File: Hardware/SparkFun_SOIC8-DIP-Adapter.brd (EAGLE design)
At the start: 20.8 x 20.8 mm, 17 parts, among them U1 GENERIC-SOIC8, U2 GENERIC-SOIC8, U3 GENERIC-SOIC8, U4 GENERIC-SOIC8

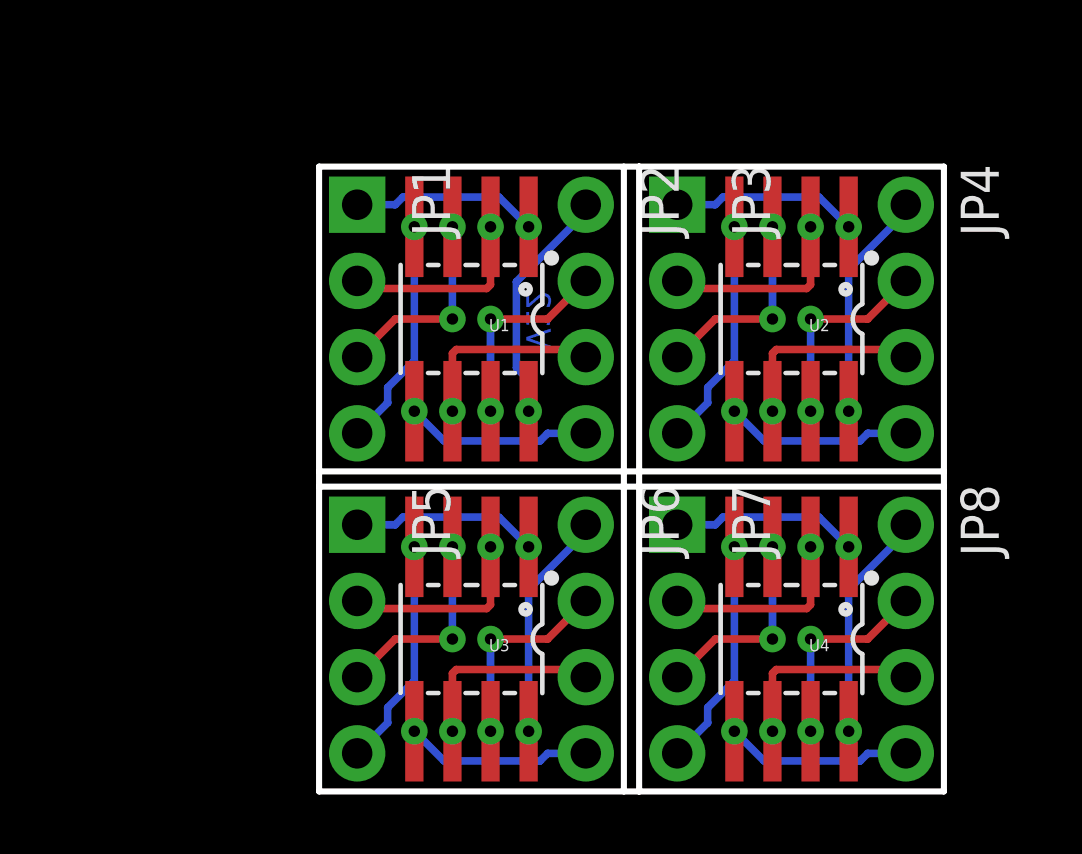
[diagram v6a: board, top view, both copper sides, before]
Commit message: added simple text to dimension layer noting v-scores
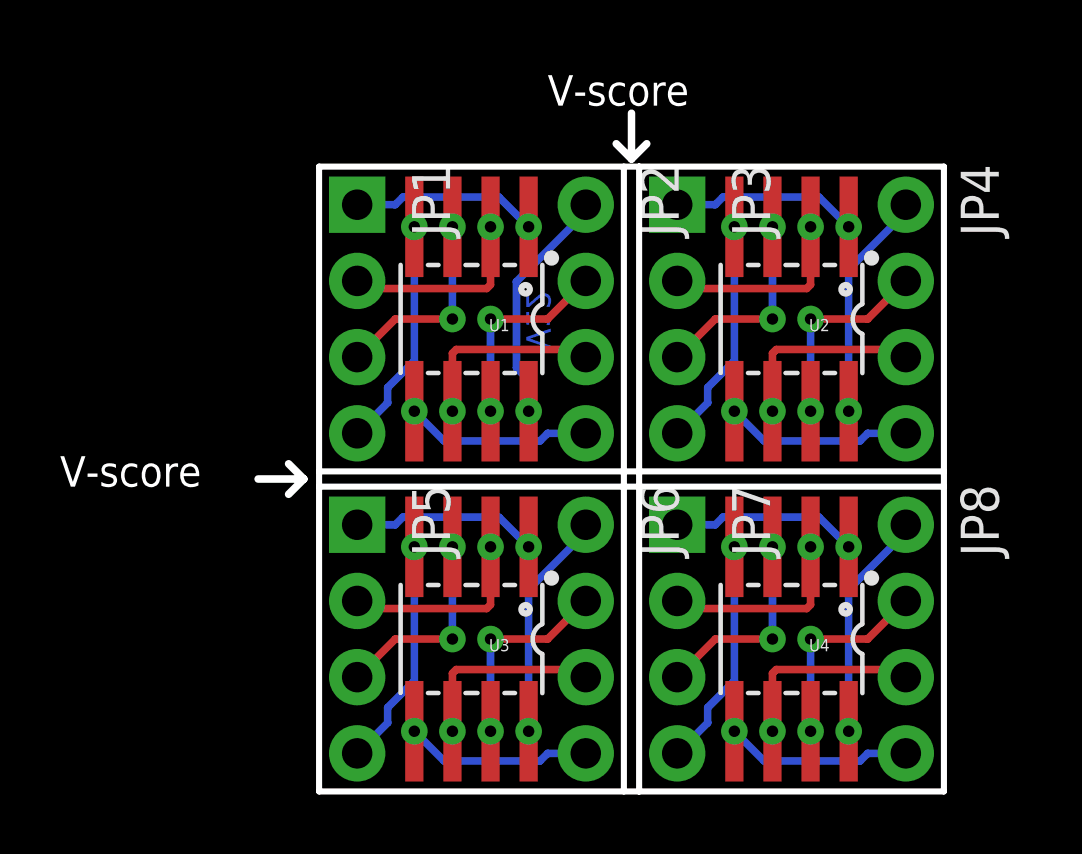
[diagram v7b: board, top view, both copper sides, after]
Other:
- board size 20.8 x 20.8 mm -> 22.9 x 22.6 mm
- board text added: "V-score"
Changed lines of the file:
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@@
 <?xml version="1.0" encoding="utf-8"?>
 <!DOCTYPE eagle SYSTEM "eagle.dtd">
-<eagle version="7.1.0">
+<eagle version="7.3.0">
 <drawing>
 <settings>
@@
 <setting verticaltext="up"/>
 </settings>
-<grid distance="0.05" unitdist="inch" unit="inch" style="lines" multiple="1" display="yes" altdistance="0.005" altunitdist="inch" altunit="inch"/>
+<grid distance="0.01" unitdist="inch" unit="inch" style="lines" multiple="1" display="yes" altdistance="0.001" altunitdist="inch" altunit="inch"/>
 <layers>
 <layer number="1" name="Top" color="4" fill="1" visible="yes" active="yes"/>
@@
 <layer number="18" name="Vias" color="2" fill="1" visible="yes" active="yes"/>
 <layer number="19" name="Unrouted" color="6" fill="1" visible="yes" active="yes"/>
-<layer number="20" name="Dimension" color="15" fill="1" visible="yes" active="yes"/>
-<layer number="21" name="tPlace" color="16" fill="1" visible="yes" active="yes"/>
-<layer number="22" name="bPlace" color="14" fill="1" visible="yes" active="yes"/>
+<layer number="20" name="Dimension" color="6" fill="1" visible="yes" active="yes"/>
+<layer number="21" name="tPlace" color="6" fill="1" visible="yes" active="yes"/>
+<layer number="22" name="bPlace" color="6" fill="1" visible="yes" active="yes"/>
 <layer number="23" name="tOrigins" color="15" fill="1" visible="yes" active="yes"/>
 <layer number="24" name="bOrigins" color="15" fill="1" visible="yes" active="yes"/>
@@
 <wire x1="20.828" y1="20.828" x2="10.668" y2="20.828" width="0.2032" layer="20"/>
 <wire x1="10.668" y1="0" x2="20.828" y2="0" width="0.2032" layer="20"/>
+<wire x1="9.906" y1="21.59" x2="10.414" y2="21.082" width="0.254" layer="20"/>
+<wire x1="10.414" y1="21.082" x2="10.922" y2="21.59" width="0.254" layer="20"/>
+<wire x1="10.414" y1="21.336" x2="10.414" y2="22.606" width="0.254" layer="20"/>
+<text x="7.62" y="22.86" size="1.016" layer="20" font="vector" ratio="7">V-score</text>
+<text x="-8.636" y="10.16" size="1.016" layer="20" font="vector" ratio="7">V-score</text>
+<wire x1="-1.016" y1="9.906" x2="-0.508" y2="10.414" width="0.254" layer="20"/>
+<wire x1="-0.508" y1="10.414" x2="-1.016" y2="10.922" width="0.254" layer="20"/>
+<wire x1="-0.762" y1="10.414" x2="-2.032" y2="10.414" width="0.254" layer="20"/>
 </plain>
 <attributes>
